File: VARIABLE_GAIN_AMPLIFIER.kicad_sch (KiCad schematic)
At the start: 33 parts, among them IC601 ${DEVICE}

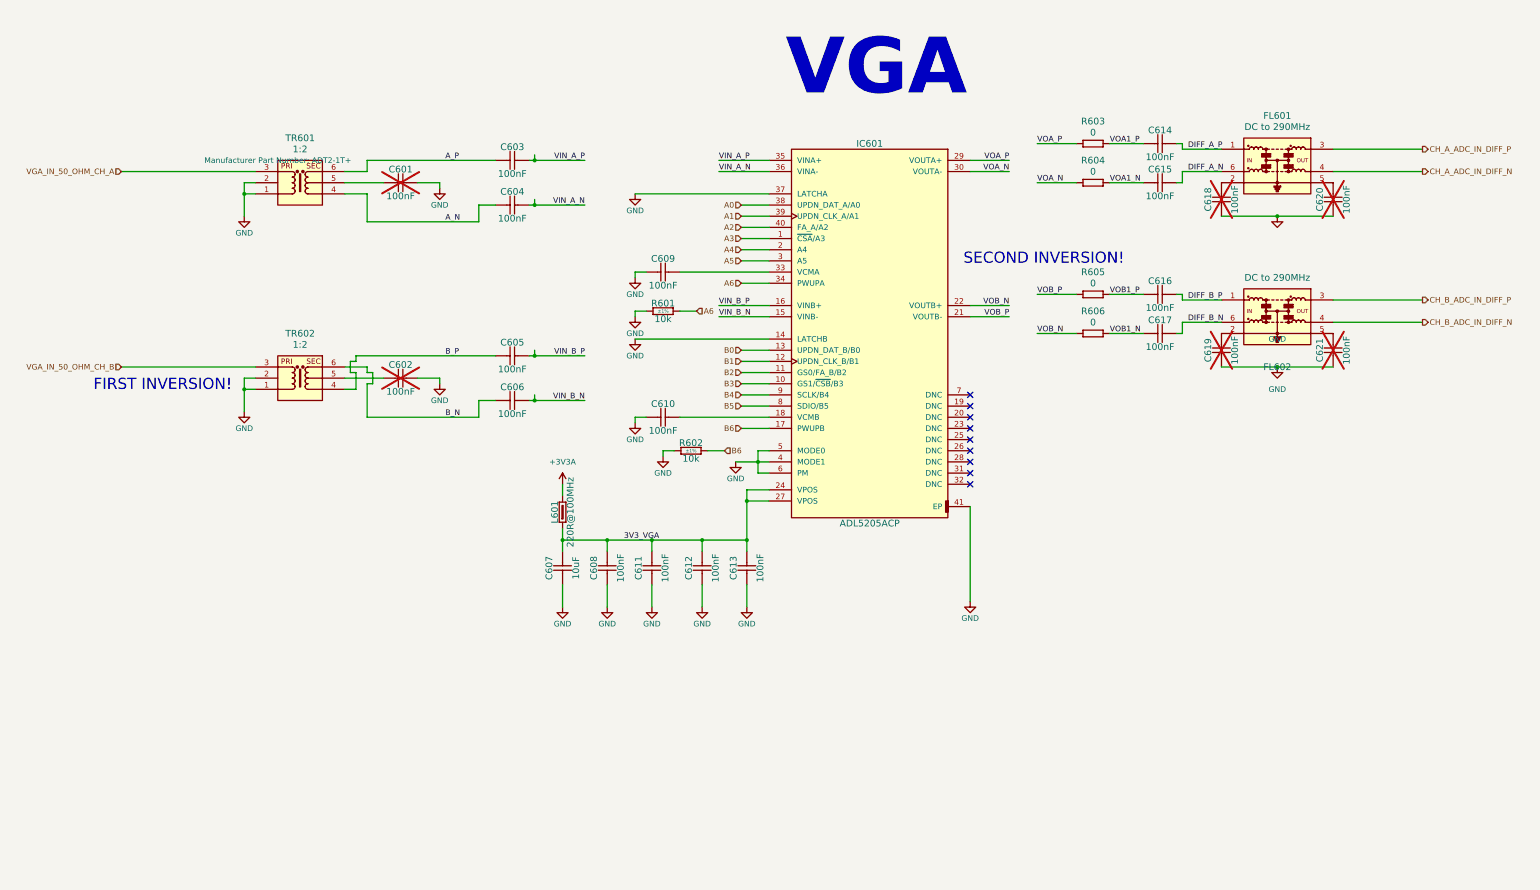
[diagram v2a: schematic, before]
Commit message: Added New LDOs
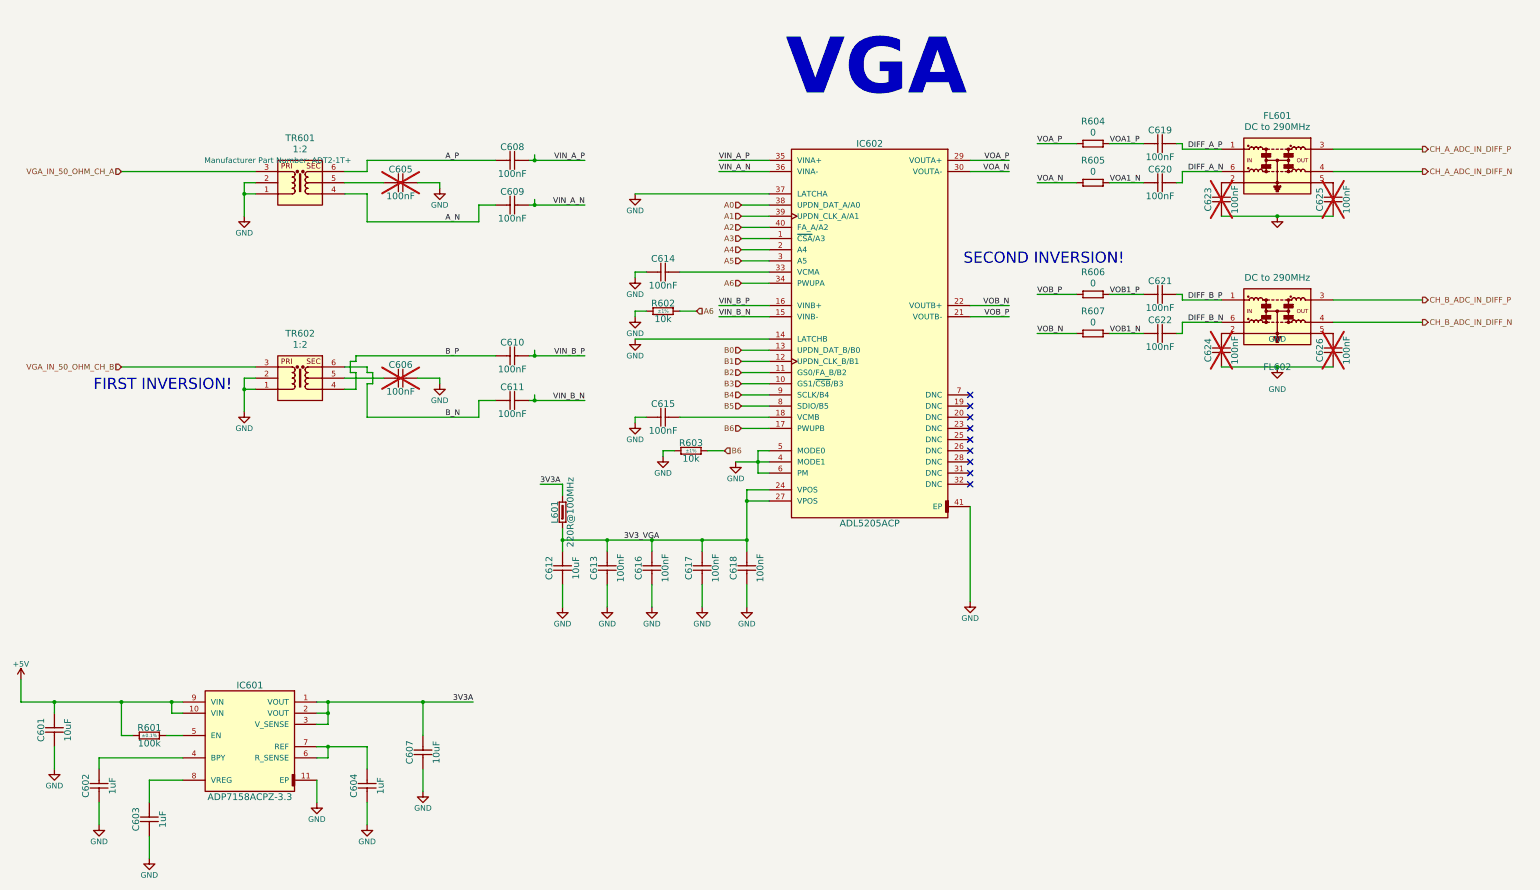
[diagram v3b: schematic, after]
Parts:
- added C601, C607: 10uF, Capacitors SMD:CAPC1608X87N, symbol CERN:Capacitors SMD/CC0603_10UF_6.3V_20%_X5R
- added C602, C603, C604: 1uF, Capacitors SMD:CAPC1608X87N, symbol CERN:Capacitors SMD/CC0603_1UF_16V_10%_X7R
- added IC601: ${DEVICE}, ICs And Semiconductors SMD:SON50P300X300X80-11N-R175X248, symbol CERN:Regulators/ADP7158ACPZ-3.3
- added R601: 100k, Resistors SMD:RESC1608X55N, symbol CERN:Resistors SMD/R0603_100K_0.1%_0.063W_10PPM
- renumbered C601 to C605, C602 to C606, C603 to C608, C604 to C609, C605 to C610, C606 to C611, C607 to C612, C608 to C613, C609 to C614, C610 to C615, C611 to C616, C612 to C617, C613 to C618, C614 to C619, C615 to C620, C616 to C621, C617 to C622, C618 to C623, C619 to C624, C620 to C625, C621 to C626, IC601 to IC602, R601 to R602, R602 to R603, R603 to R604, R604 to R605, R605 to R606, R606 to R607
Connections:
- net GND: now also C601.1, C602.1, C603.1, C604.1, C607.1, IC601.11 (EP)
- net +3V3A renamed 3V3A
- net 3V3A: now also C607.2, IC601.1 (VOUT), IC601.2 (VOUT), IC601.3 (V_SENSE)
- new net: C602.2, IC601.4 (BPY)
- new net: IC601.5 (EN), R601.2
- new net: C604.2, IC601.6 (R_SENSE), IC601.7 (REF)
- new net: C603.2, IC601.8 (VREG)
- new net +5V: C601.2, IC601.10 (VIN), IC601.9 (VIN), R601.1

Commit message: Update project files and backups
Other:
- note added: "Note on power dissipation on 3V3A: ADL5205 takes 175 mA Iccq + 2 * 20 mA output short circuit current = ~250 mA Ptot = (3.3V - 5.5V) * 250 mA = 0.55 W"
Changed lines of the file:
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@@
 		(comment 1 "Design by A. Jevtic")
+	)
+	(text "Note on power dissipation on 3V3A:\n\nADL5205 takes 175 mA Iccq + 2 * 20 mA output short circuit current = ~250 mA\n\nPtot = (3.3V - 5.5V) * 250 mA = 0.55 W"
+		(exclude_from_sim no)
+		(at 83.058 211.582 0)
+		(effects
+			(font
+				(size 1.27 1.27)
+			)
+		)
 	)
 	(text "SECOND INVERSION!"
@@
 			(pts
 				(xy 260.35 146.05) (xy 260.35 128.27) (xy 298.45 128.27) (xy 298.45 130.81) (xy 372.11 130.81) (xy 372.11 146.05)
+				(xy 335.28 146.05) (xy 335.28 138.43) (xy 299.72 138.43) (xy 299.72 146.05)
 			)
 			(stroke
@@
 			(justify right bottom)
 		)
-		(property "Netclass" "100_OHM"
+		(property "Netclass" "ZDIFF_100_OHM"
 			(at 111.6965 161.29 0)
 			(effects
@@
 			(justify left bottom)
 		)
-		(property "Netclass" "100_OHM"
+		(property "Netclass" "ZDIFF_100_OHM"
 			(at 149.7965 151.13 0)
 			(effects
@@
 			(justify left bottom)
 		)
-		(property "Netclass" "100_OHM"
+		(property "Netclass" "ZDIFF_100_OHM"
 			(at 109.1565 142.24 0)
 			(effects
@@
 			(justify left bottom)
 		)
-		(property "Netclass" "100_OHM"
+		(property "Netclass" "ZDIFF_100_OHM"
 			(at 111.6965 97.79 0)
 			(effects
@@
 			(justify left bottom)
 		)
-		(property "Netclass" "100_OHM"
+		(property "Netclass" "ZDIFF_100_OHM"
 			(at 149.7965 106.68 0)
 			(effects
@@
 			(justify left bottom)
 		)
-		(property "Netclass" "100_OHM"
+		(property "Netclass" "ZDIFF_100_OHM"
 			(at 261.5565 86.36 0)
 			(effects
@@
 			(justify left bottom)
 		)
-		(property "Netclass" "100_OHM"
+		(property "Netclass" "ZDIFF_100_OHM"
 			(at 149.7965 140.97 0)
 			(effects
@@
 			(justify right bottom)
 		)
-		(property "Netclass" "100_OHM"
+		(property "Netclass" "ZDIFF_100_OHM"
 			(at 111.6965 116.84 0)
 			(effects
@@
 			(justify right bottom)
 		)
-		(property "Netclass" "100_OHM"
+		(property "Netclass" "ZDIFF_100_OHM"
 			(at 261.5565 148.59 0)
 			(effects
@@
 			(justify left bottom)
 		)
-		(property "Netclass" "100_OHM"
+		(property "Netclass" "ZDIFF_100_OHM"
 			(at 149.7965 96.52 0)
 			(effects
